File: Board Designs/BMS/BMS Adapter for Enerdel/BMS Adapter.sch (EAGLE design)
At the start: 23 parts

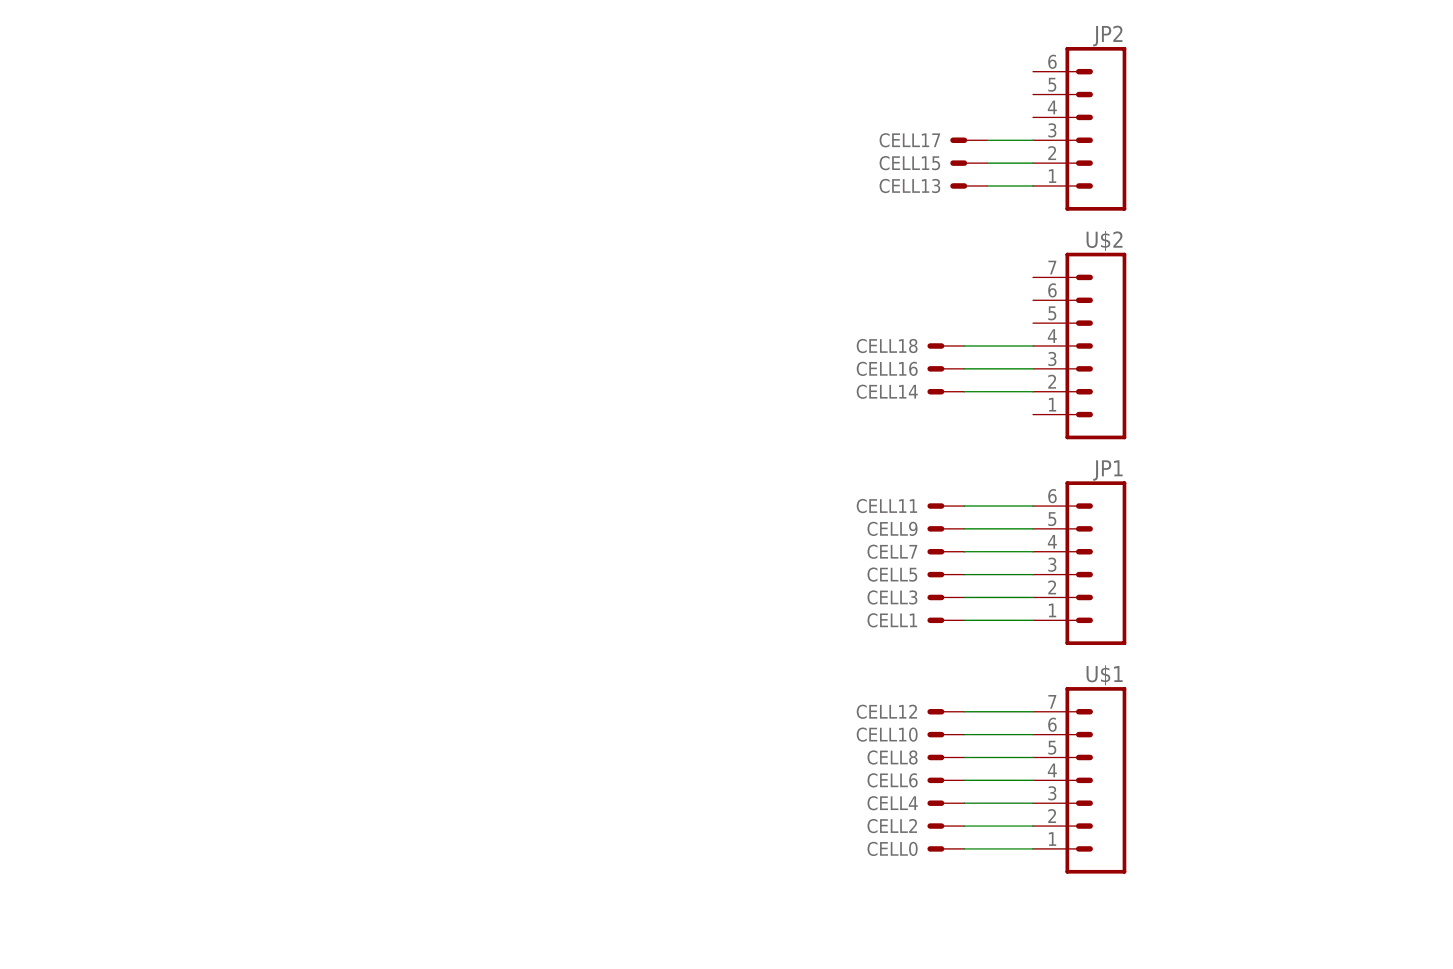
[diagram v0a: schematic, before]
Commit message: added Adapter file
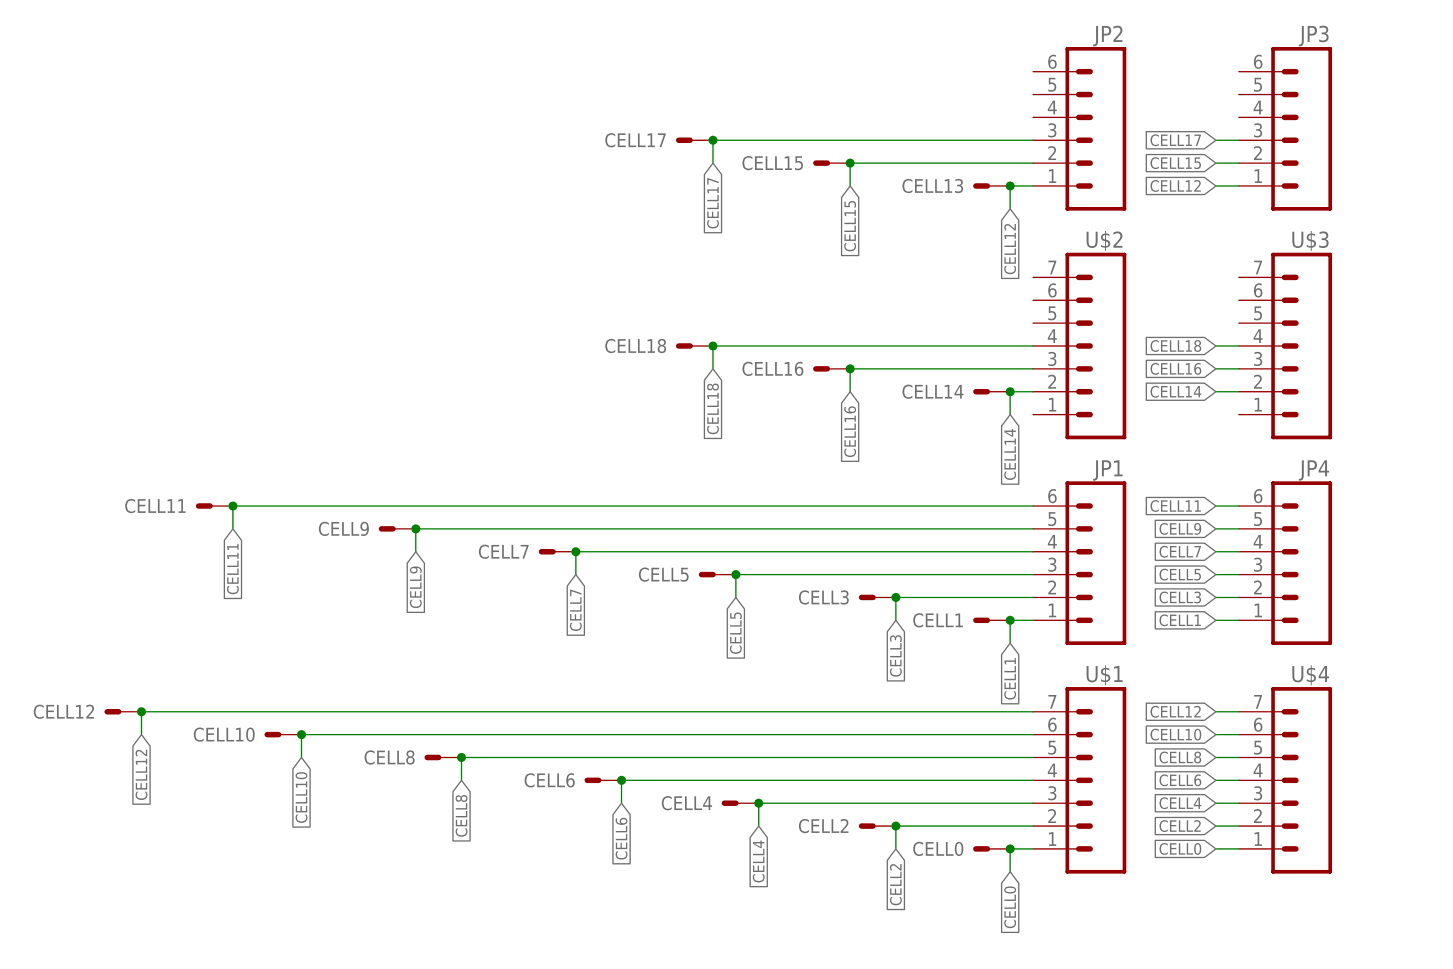
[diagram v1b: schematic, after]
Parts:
- added JP3, JP4: (no value), HyTechDevices:M06
- added U$3, U$4: M07, HyTechDevices:M07
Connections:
- removed net N$1: CELL0.S, U$1.1
- removed net N$10: CELL5.S, JP1.3
- removed net N$11: CELL7.S, JP1.4
- removed net N$12: CELL9.S, JP1.5
- removed net N$13: CELL11.S, JP1.6
- removed net N$14: CELL18.S, U$2.4
- removed net N$15: CELL16.S, U$2.3
- removed net N$16: CELL14.S, U$2.2
- removed net N$17: CELL13.S, JP2.1
- removed net N$18: CELL15.S, JP2.2
- removed net N$19: CELL17.S, JP2.3
- removed net N$2: CELL2.S, U$1.2
- removed net N$3: CELL4.S, U$1.3
- removed net N$4: CELL6.S, U$1.4
- removed net N$5: CELL8.S, U$1.5
- removed net N$6: CELL10.S, U$1.6
- removed net N$7: CELL12.S, U$1.7
- removed net N$8: CELL1.S, JP1.1
- removed net N$9: CELL3.S, JP1.2
- new net CELL0: CELL0.S, U$1.1, U$4.1
- new net CELL1: CELL1.S, JP1.1, JP4.1
- new net CELL10: CELL10.S, U$1.6, U$4.6
- new net CELL11: CELL11.S, JP1.6, JP4.6
- new net CELL12: CELL12.S, CELL13.S, JP2.1, JP3.1, U$1.7, U$4.7
- new net CELL14: CELL14.S, U$2.2, U$3.2
- new net CELL15: CELL15.S, JP2.2, JP3.2
- new net CELL16: CELL16.S, U$2.3, U$3.3
- new net CELL17: CELL17.S, JP2.3, JP3.3
- new net CELL18: CELL18.S, U$2.4, U$3.4
- new net CELL2: CELL2.S, U$1.2, U$4.2
- new net CELL3: CELL3.S, JP1.2, JP4.2
- new net CELL4: CELL4.S, U$1.3, U$4.3
- new net CELL5: CELL5.S, JP1.3, JP4.3
- new net CELL6: CELL6.S, U$1.4, U$4.4
- new net CELL7: CELL7.S, JP1.4, JP4.4
- new net CELL8: CELL8.S, U$1.5, U$4.5
- new net CELL9: CELL9.S, JP1.5, JP4.5
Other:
- moved on the sheet: CELL0, CELL1, CELL10, CELL11, CELL12, CELL13, CELL14, CELL15, CELL16, CELL17, CELL18, CELL2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

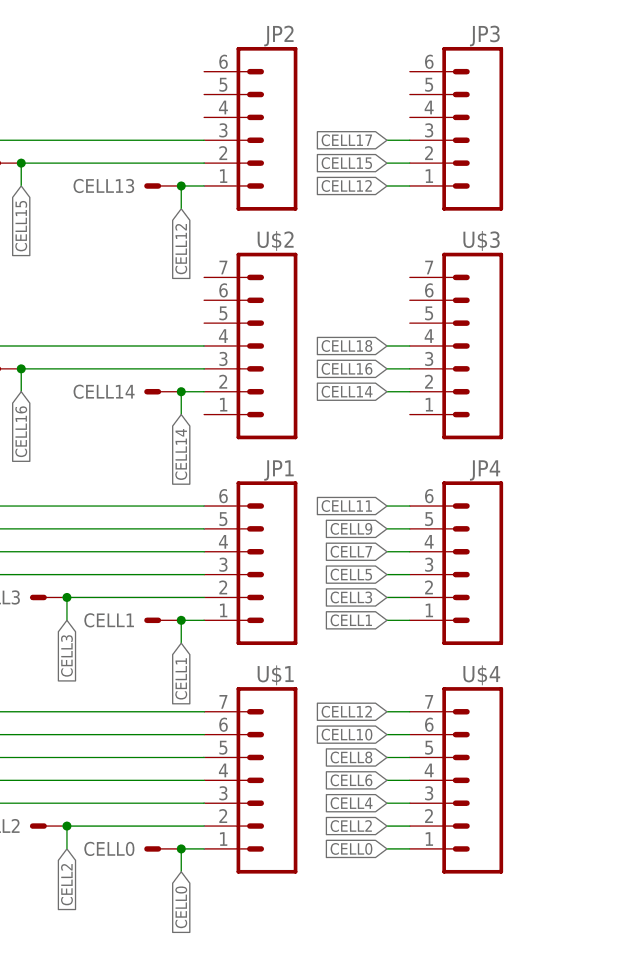
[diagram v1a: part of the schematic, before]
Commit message: Changed adapter board to include minifit connectors.
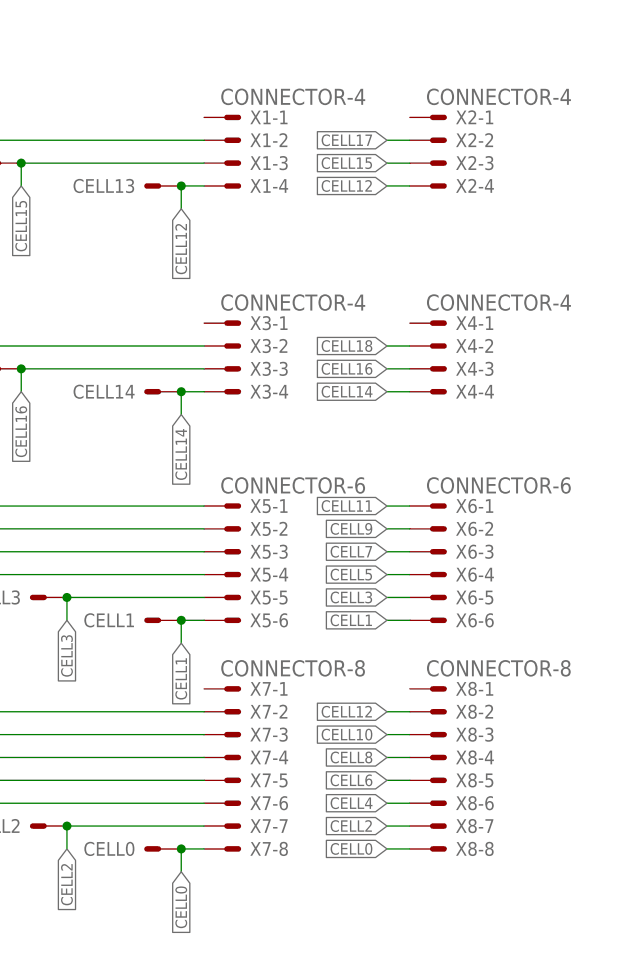
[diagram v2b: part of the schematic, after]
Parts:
- removed JP1, JP2, JP3, JP4: (no value), HyTechDevices:M06
- removed U$1, U$2, U$3, U$4: M07, HyTechDevices:M07
- added X1, X2, X3, X4: CONNECTOR-4, HyTechDevices:CONNECTOR-4
- added X5, X6: CONNECTOR-6, HyTechDevices:CONNECTOR-6
- added X7, X8: CONNECTOR-8, HyTechDevices:CONNECTOR-8
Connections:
- net CELL0: now also X7-8.S, X8-8.S; no longer U$1.1, U$4.1
- net CELL1: now also X5-6.S, X6-6.S; no longer JP1.1, JP4.1
- net CELL10: now also X7-3.S, X8-3.S; no longer U$1.6, U$4.6
- net CELL11: now also X5-1.S, X6-1.S; no longer JP1.6, JP4.6
- net CELL12: now also X1-4.S, X2-4.S, X7-2.S, X8-2.S; no longer JP2.1, JP3.1, U$1.7, U$4.7
- net CELL14: now also X3-4.S, X4-4.S; no longer U$2.2, U$3.2
- net CELL15: now also X1-3.S, X2-3.S; no longer JP2.2, JP3.2
- net CELL16: now also X3-3.S, X4-3.S; no longer U$2.3, U$3.3
- net CELL17: now also X1-2.S, X2-2.S; no longer JP2.3, JP3.3
- net CELL18: now also X3-2.S, X4-2.S; no longer U$2.4, U$3.4
- net CELL2: now also X7-7.S, X8-7.S; no longer U$1.2, U$4.2
- net CELL3: now also X5-5.S, X6-5.S; no longer JP1.2, JP4.2
- net CELL4: now also X7-6.S, X8-6.S; no longer U$1.3, U$4.3
- net CELL5: now also X5-4.S, X6-4.S; no longer JP1.3, JP4.3
- net CELL6: now also X7-5.S, X8-5.S; no longer U$1.4, U$4.4
- net CELL7: now also X5-3.S, X6-3.S; no longer JP1.4, JP4.4
- net CELL8: now also X7-4.S, X8-4.S; no longer U$1.5, U$4.5
- net CELL9: now also X5-2.S, X6-2.S; no longer JP1.5, JP4.5
